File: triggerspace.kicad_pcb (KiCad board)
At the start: 2 copper layers, 257.6 x 128.5 mm, 161 parts, among them J1 Conn_01x2, J10 Conn_01x12, J11 Conn_01x12, J12 Conn_02x05_Odd_Even, J13 Conn_01x10, J14 Conn_01x10, J15 Conn_01x10, J2 Conn_01x2, J3 Conn_01x4, J4 Conn_01x2, J4 Conn_01x4, J5 Conn_01x3, J6 Conn_01x3, J7 Conn_01x10, J8 Conn_01x3, Q1 2N3904, Q2 2N3904, U1 MCP6002_1, U2 MCP6002_1, U3 MCP6002_1, U4 L7805, U5 LM4040LP-5, U6 74HC595, U8 6N138, X1 CV_X, Y1 CV_Y

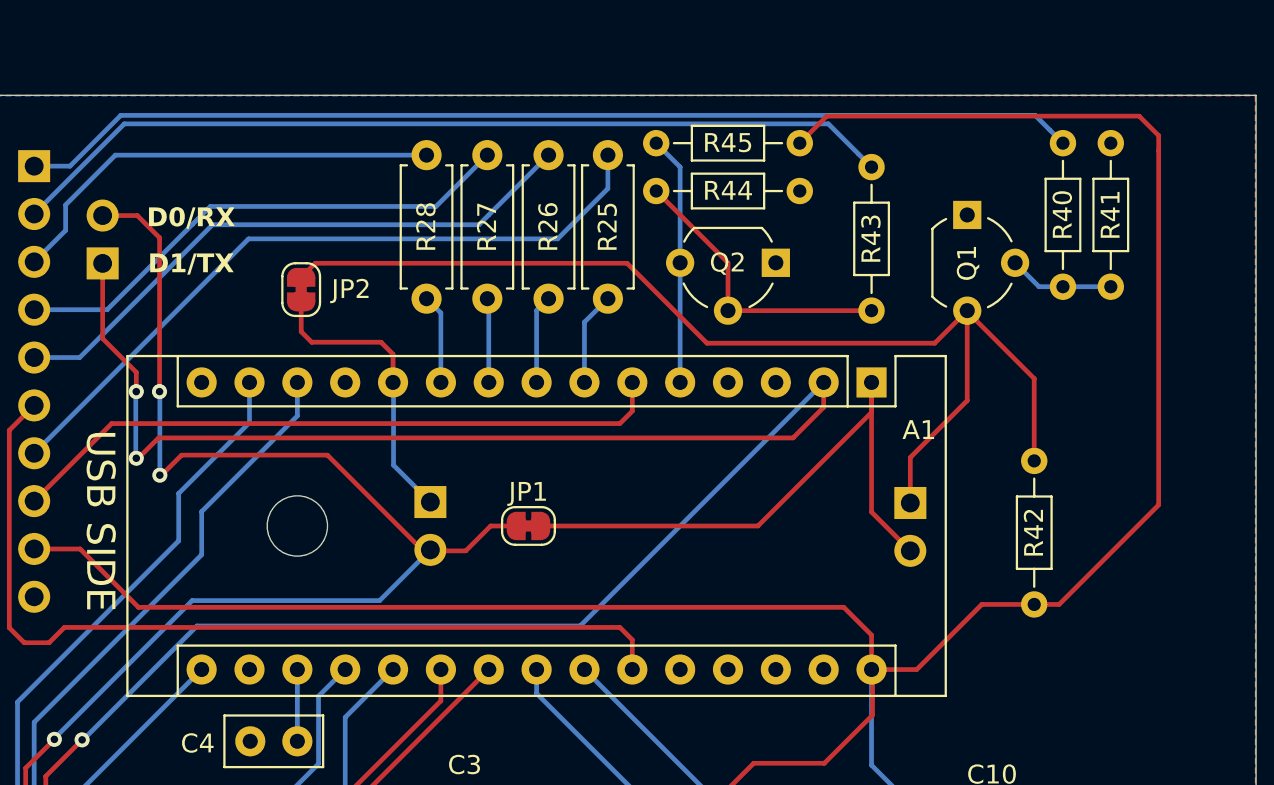
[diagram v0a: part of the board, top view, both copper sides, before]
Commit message: Hardware: PCB layout revision, aluminium front-panel gerbers, panel SVG
Update the main PCB layout, add the aluminium front-panel fabrication
outputs (production/front_panel_aluminium/) and panel cutout artwork (svg/).
README roadmap notes: LPZW_TRS_MIDI dual-type-A/B option; fix a typo.

(PCB layout authored in KiCad; committed as-is.)
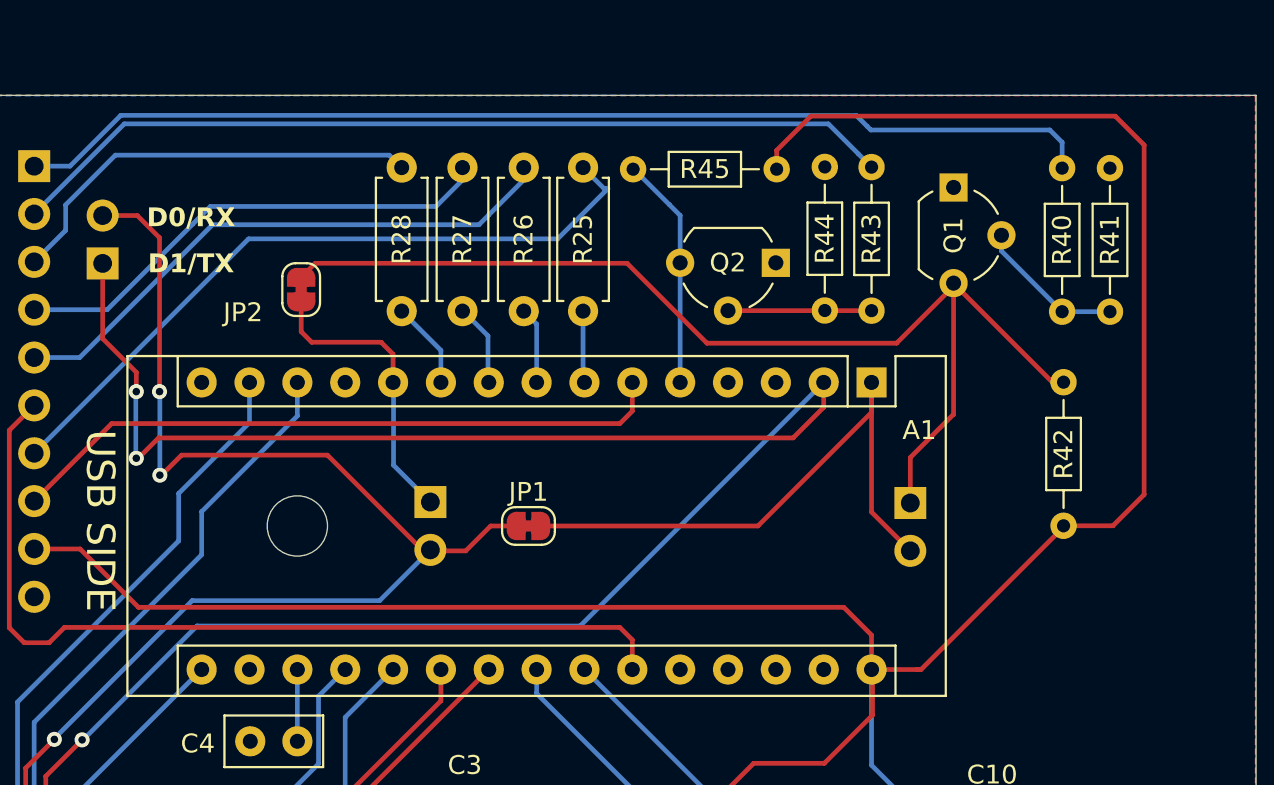
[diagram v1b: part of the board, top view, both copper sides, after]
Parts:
- moved R44 11.0 mm to (146.1, 29.2), turned to 90 degrees
- moved R42 4.46 mm to (158.8, 40.6)
- moved R45 1.85 mm to (143.6, 21.7)
- moved Q1 1.63 mm to (152.9, 22.7)
- moved R25 1.48 mm to (133.3, 29.2)
- moved R26 1.48 mm to (130.1, 29.2)
- moved R27 1.48 mm to (126.9, 29.2)
- moved R28 1.48 mm to (123.6, 29.2)
- moved R40 1.33 mm to (158.7, 29.3)
- moved R41 1.33 mm to (161.2, 29.3)
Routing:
- net Net-(Q2-B): track 15.5 -> 7.62 mm
- net Net-(Q1-B): track 5.61 -> 7.93 mm
- net J_CLK: track 115.8 -> 117.1 mm
- net LED_CH2: track 102.7 -> 101.5 mm
- net LED_CH3: track 91.0 -> 89.8 mm
- net Net-(A1-D4): track 4.96 -> 3.81 mm
- net LED_CH1: track 115.1 -> 114.1 mm
- net IN_RESET: track 13.2 -> 12.4 mm
- net Net-(A1-D5): track 4.71 -> 4.07 mm

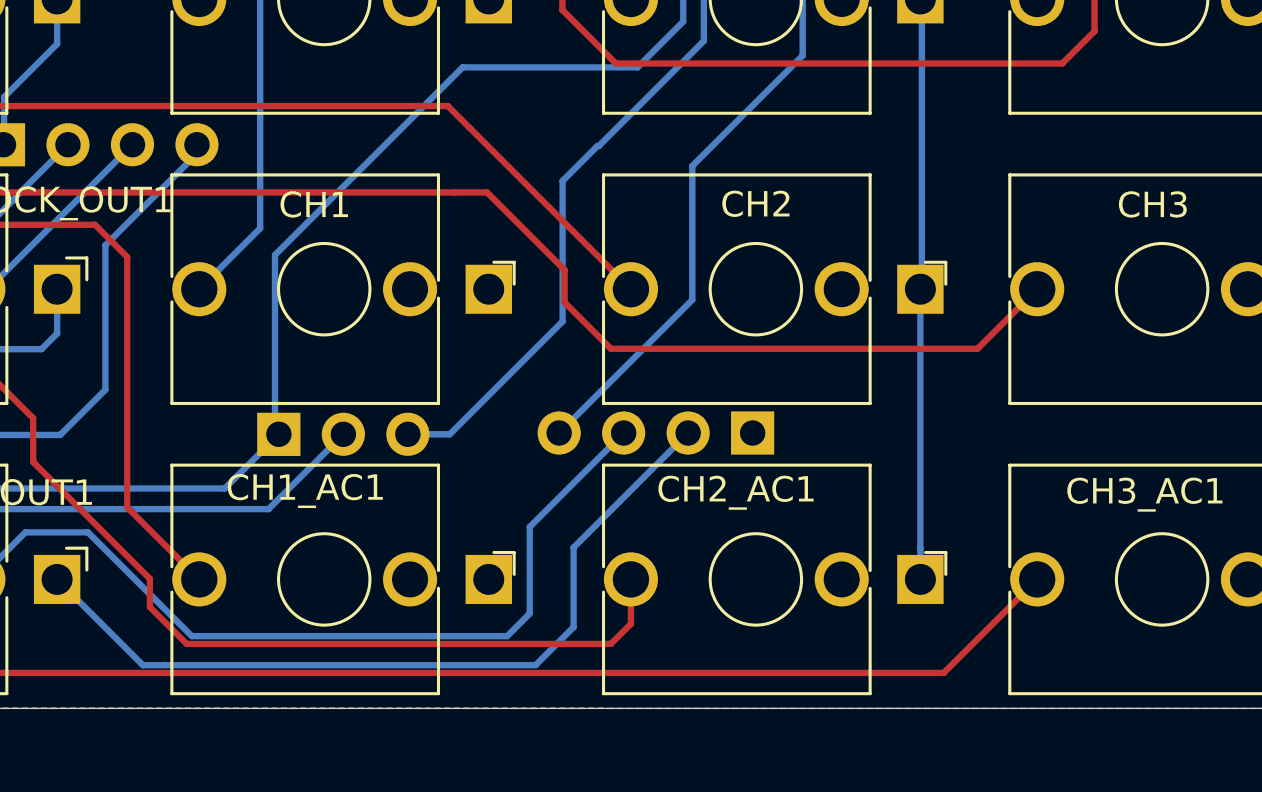
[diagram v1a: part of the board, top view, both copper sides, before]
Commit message: Hardware: socketed RC reconstruction caps on the six output jacks
Adds J16..J21 (2.54mm 1x02 sockets) on the jack PCB's back copper, one per
audio output jack. Pin 1 taps the channel net on the jack side of the 1k
series resistor (R32..R37 on the back board); pin 2 lands in the GND pour.
Plugging a capacitor in forms a first-order reconstruction low-pass with the
existing 1k; pulling it out disables the filter, so the cap value stays a
run-time choice rather than a layout commitment.

J16 CH1, J17 CH2, J18 CH3, J19 CH1_ACC, J20 CH2_ACC, J21 CH3_ACC.

The 1k resistors are unchanged - they already set the expected ~1k Eurorack
output impedance and double as the filter's series R.

Placement was clearance-solved against existing pads, tracks and courtyards;
each socket routes to its jack tip pad with a single 2.24mm B.Cu track, and
GND needs no routing (full GND zones on both layers). Socket outlines moved
to B.Fab as the back silkscreen is congested there.

Note: pcbnew 9 re-serialised the .kicad_pcb (KiCad 8 -> 9 format) and
refilled the zones, which cleared pre-existing stale-fill DRC violations.
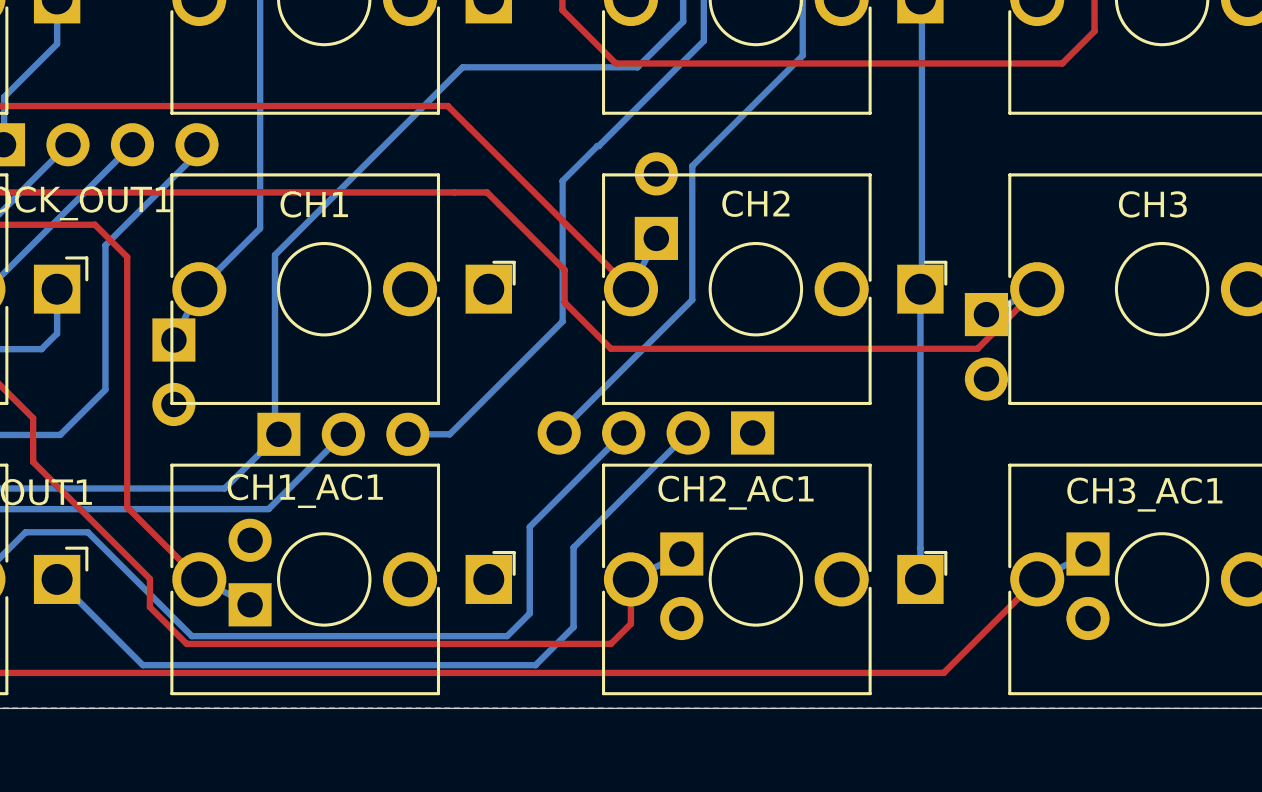
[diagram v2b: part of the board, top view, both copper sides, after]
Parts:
- added J16: Conn_01x2, Connector_PinSocket_2.54mm:PinSocket_1x02_P2.54mm_Vertical, B.Cu at (219.0, 111.2)
- added J17: Conn_01x2, Connector_PinSocket_2.54mm:PinSocket_1x02_P2.54mm_Vertical, B.Cu at (238.0, 107.2)
- added J18: Conn_01x2, Connector_PinSocket_2.54mm:PinSocket_1x02_P2.54mm_Vertical, B.Cu at (251.0, 110.2)
- added J19: Conn_01x2, Connector_PinSocket_2.54mm:PinSocket_1x02_P2.54mm_Vertical, B.Cu at (222.0, 121.7)
- added J20: Conn_01x2, Connector_PinSocket_2.54mm:PinSocket_1x02_P2.54mm_Vertical, B.Cu at (239.0, 119.7)
- added J21: Conn_01x2, Connector_PinSocket_2.54mm:PinSocket_1x02_P2.54mm_Vertical, B.Cu at (255.0, 119.7)
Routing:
- net CH3_ACC: track 108.9 -> 111.2 mm
- net CH2_ACC: track 97.6 -> 99.8 mm
- net CH1_ACC: track 88.0 -> 90.2 mm
- net CH3: track 117.4 -> 119.6 mm
- net CH1: track 112.1 -> 114.3 mm
- net CH2: track 105.0 -> 107.2 mm

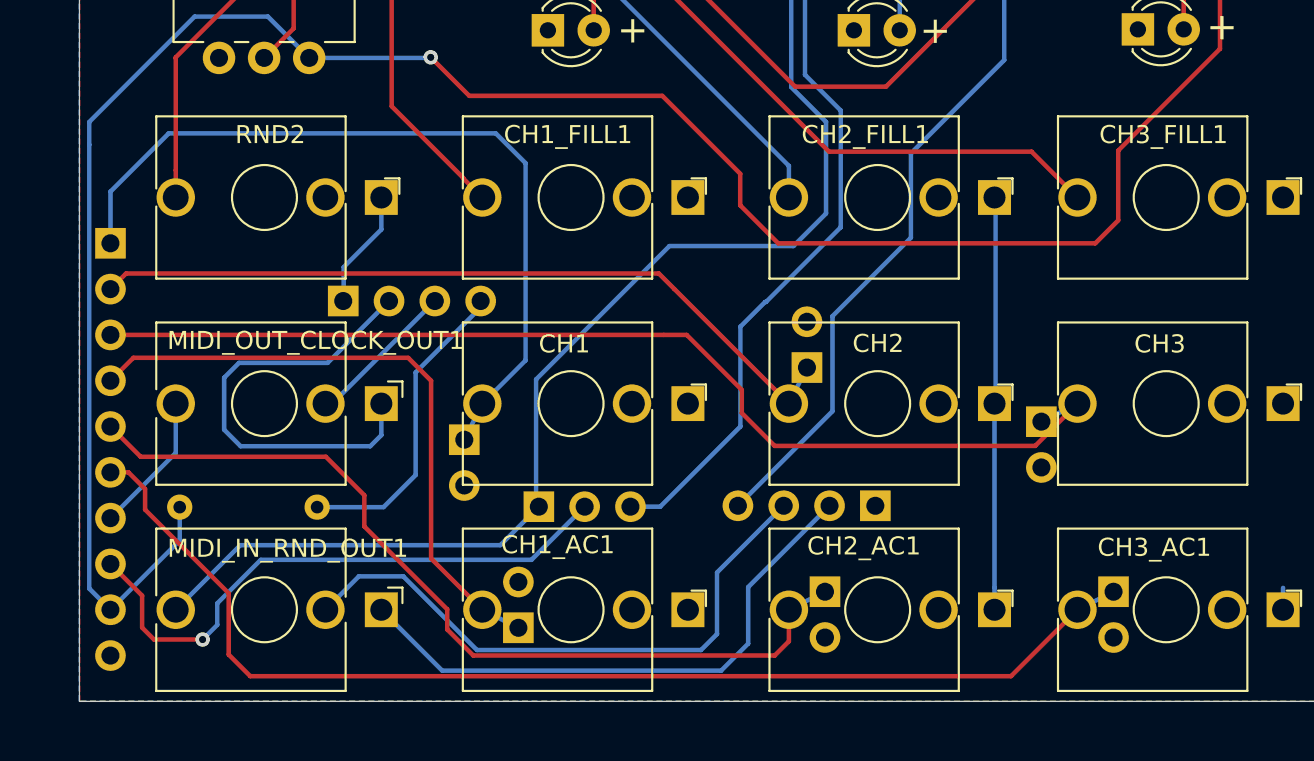
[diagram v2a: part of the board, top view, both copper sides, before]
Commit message: Fixed cap socket placement by hand
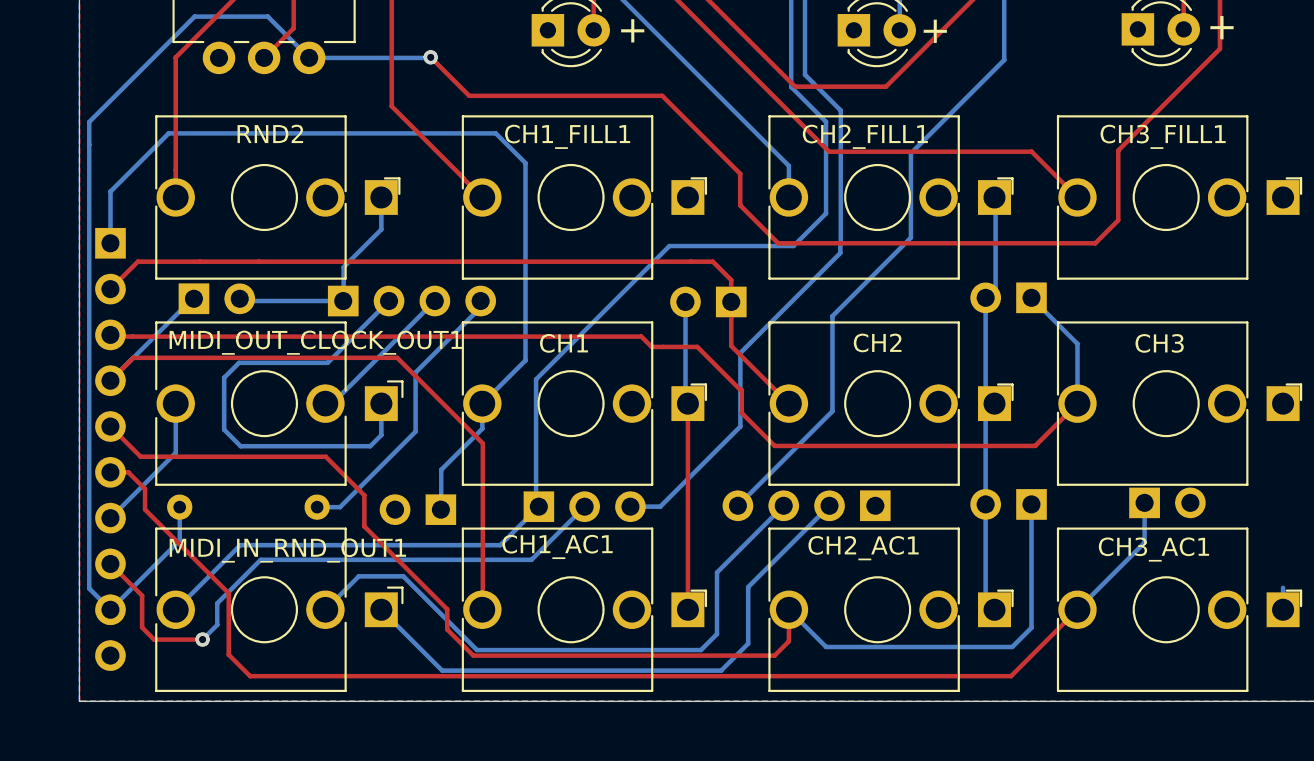
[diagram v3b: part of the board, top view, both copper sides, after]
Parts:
- moved CH1_ACC_CAP 25.6 mm to (204.0, 103.4), turned to -90 degrees
- moved CH2_ACC_CAP 12.4 mm to (250.5, 114.8), turned to 90 degrees
- moved CH3_CAP 6.89 mm to (250.5, 103.4), turned to 90 degrees
- moved CH2_CAP 5.55 mm to (233.8, 103.6), turned to 90 degrees
- moved CH3_ACC 5.22 mm to (256.7, 114.7), turned to -90 degrees
- moved CH1_CAP 4.09 mm to (217.7, 115.1), turned to 90 degrees
- renumbered J19 to CH1_ACC_CAP, J16 to CH1_CAP, J20 to CH2_ACC_CAP, J17 to CH2_CAP, J21 to CH3_ACC, J18 to CH3_CAP
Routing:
- net GND: track 110.8 -> 134.6 mm
- net CH2_ACC: track 99.8 -> 119.2 mm
- net CH3_ACC: track 111.2 -> 116.4 mm
- net CH3: track 119.6 -> 124.3 mm
- net CH1: track 114.3 -> 118.9 mm
- net CH1_ACC: track 90.2 -> 94.1 mm
- net Net-(J3-Pin_4): track 17.3 -> 15.9 mm

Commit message: Bump version to v0.5.0, regenerate back_pcb/jack_pcb fab outputs
Version bump (schematic title-block rev, PCB silkscreen text on both boards)
reflects the RC reconstruction-cap sockets added on the jack PCB's six audio
outputs. README documents the new revision as pending bench verification,
keeping the v0.042 notes as historical build/bodge record.

Regenerated gerbers, drill, position files, netlist, and BOM for back_pcb and
jack_pcb to pick up the cap-socket placement fix and the new silkscreen text.
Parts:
- renumbered CH1_ACC_CAP to CH1_ACC_CAP1, CH1_CAP to CH1_CAP1, CH2_ACC_CAP to CH2_ACC_CAP1, CH2_CAP to CH2_CAP1, CH3_ACC to CH3_ACC_CAP1, CH3_CAP to CH3_CAP1
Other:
- board text added: "NanoGris-MIDI V0.5.0"
- board text removed: "NanoGris-MIDI V0.042"
